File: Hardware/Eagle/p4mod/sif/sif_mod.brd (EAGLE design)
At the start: 19.1 x 11.6 mm, 37 parts, among them Q1 IRLML0030, Q2 IRLML0030, Q3 IRLML0030, Q4 IRLML0030

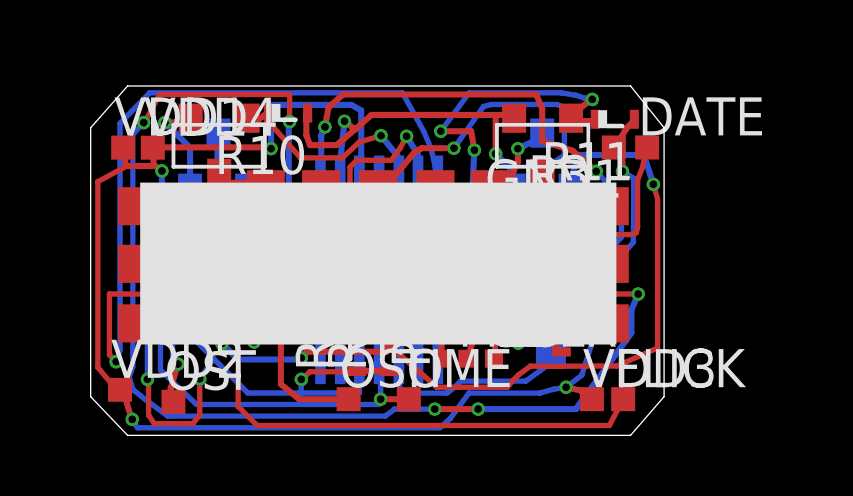
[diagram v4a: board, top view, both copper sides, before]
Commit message: Improved segment resistor values.
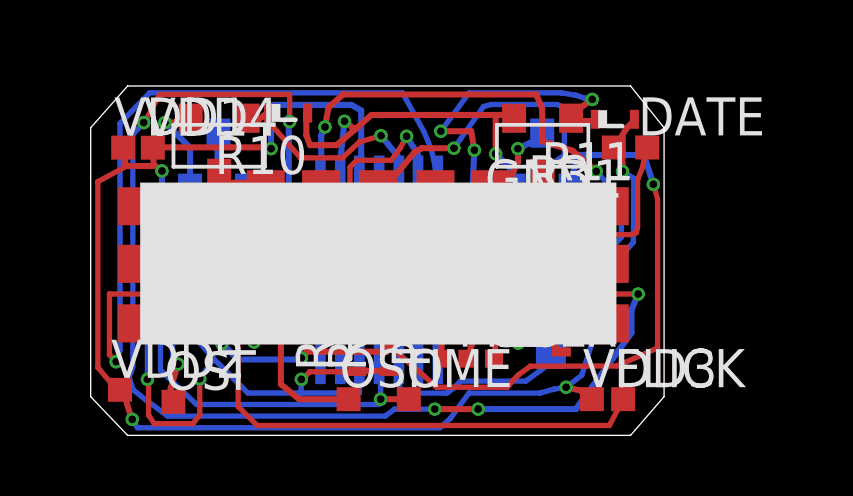
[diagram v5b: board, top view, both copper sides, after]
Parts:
- R2, R3, R4, R5, R6, R7, R8: value 82 -> 75
- moved C1 0.20 mm to (5.05, 4.16)
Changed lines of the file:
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@@
 </element>
 <element name="R1" library="resistor_mod" package="R0402" value="10K" x="18.35831875" y="4.3688" rot="MR90"/>
-<element name="C2" library="resistor_mod" package="C0402K" value="0.1 uF" x="4.553640625" y="7.308175" rot="MR180"/>
+<element name="C2" library="resistor_mod" package="C0402K" value="0.1 uF" x="4.553640625" y="7.3348625" rot="MR180"/>
 <element name="CEFC" library="rcl" package="C0603" value="10 uF" x="16.90450625" y="3.814696875" rot="MR90"/>
-<element name="R2" library="resistor_mod" package="R0402" value="82" x="13.008109375" y="6.29623125"/>
-<element name="R3" library="resistor_mod" package="R0402" value="82" x="16.778290625" y="7.4951875"/>
-<element name="R4" library="resistor_mod" package="R0402" value="82" x="5.038421875" y="4.174128125" rot="R270"/>
-<element name="R5" library="resistor_mod" package="R0402" value="82" x="17.252953125" y="5.629190625" rot="R90"/>
-<element name="R6" library="resistor_mod" package="R0402" value="82" x="17.252953125" y="3.62104375" rot="R90"/>
-<element name="R7" library="resistor_mod" package="R0402" value="82" x="4.9276" y="6.174871875" rot="R270"/>
-<element name="R8" library="resistor_mod" package="R0402" value="82" x="9.549" y="6.708275" rot="R180"/>
+<element name="R2" library="resistor_mod" package="R0402" value="75" x="13.008109375" y="6.29623125"/>
+<element name="R3" library="resistor_mod" package="R0402" value="75" x="16.778290625" y="7.4951875"/>
+<element name="R4" library="resistor_mod" package="R0402" value="75" x="5.038421875" y="4.174128125" rot="R270"/>
+<element name="R5" library="resistor_mod" package="R0402" value="75" x="17.252953125" y="5.629190625" rot="R90"/>
+<element name="R6" library="resistor_mod" package="R0402" value="75" x="17.252953125" y="3.62104375" rot="R90"/>
+<element name="R7" library="resistor_mod" package="R0402" value="75" x="4.9276" y="6.174871875" rot="R270"/>
+<element name="R8" library="resistor_mod" package="R0402" value="75" x="9.549" y="6.708275" rot="R180"/>
 <element name="C4" library="resistor_mod" package="C0402K" value="12 pF" x="4.85618125" y="6.03475" rot="MR90"/>
 <element name="R16" library="resistor_mod" package="R0402" value="4.7k" x="18.35831875" y="6.402271875" rot="MR270"/>
@@
 <attribute name="TP_SIGNAL_NAME" value="" x="18.9992" y="9.787525" size="1.778" layer="27" rot="R180" display="off"/>
 </element>
-<element name="C1" library="resistor_mod" package="C0402K" value="12 pF" x="4.84966875" y="4.17638125" rot="MR270"/>
+<element name="C1" library="resistor_mod" package="C0402K" value="12 pF" x="5.049746875" y="4.1630375" rot="MR270"/>
 <element name="U$2" library="pulsar_p4_display" package="PULSAR_P3_LED_DISPLAY" value="PULSAR_P4_DISPLAYPULSAR_P4_LED_DISPLAY" x="3.21241875" y="3.21965625"/>
 <element name="VDD2" library="testpad" package="TP08SQ" value="TPTP08SQ" x="2.5390625" y="1.708484375">
@@
 <wire x1="5.1308" y1="7.2898" x2="5.1308" y2="6.9088" width="0.2032" layer="16"/>
 <wire x1="4.8768" y1="6.6548" x2="4.85618125" y2="6.63475" width="0.1524" layer="16"/>
-<wire x1="5.1308" y1="7.2898" x2="5.153640625" y2="7.308175" width="0.1524" layer="16"/>
+<wire x1="5.1308" y1="7.2898" x2="5.153640625" y2="7.3348625" width="0.1524" layer="16"/>
 <wire x1="4.8006" y1="6.6548" x2="4.0894" y2="6.6548" width="0.2032" layer="16"/>
 <wire x1="4.0894" y1="6.6548" x2="4.07449375" y2="6.649225" width="0.1524" layer="16"/>
@@
 <wire x1="5.1054" y1="7.366" x2="5.1054" y2="8.4074" width="0.2032" layer="16"/>
 <wire x1="4.9022" y1="8.6106" x2="4.875296875" y2="8.429753125" width="0.1524" layer="16"/>
-<wire x1="5.1054" y1="7.366" x2="5.153640625" y2="7.308175" width="0.2032" layer="16"/>
+<wire x1="5.1054" y1="7.366" x2="5.153640625" y2="7.3348625" width="0.2032" layer="16"/>
 <wire x1="4.4040625" y1="10.62851875" x2="4.8768" y2="10.4648" width="0.2032" layer="1"/>
 <wire x1="4.0386" y1="10.6172" x2="4.4040625" y2="10.62851875" width="0.2032" layer="1"/>
@@
 <wire x1="11.4808" y1="2.3368" x2="11.504365625" y2="2.32038125" width="0.1524" layer="1"/>
 <wire x1="6.80068125" y1="1.604009375" x2="5.6642" y2="2.7432" width="0.1778" layer="16"/>
-<wire x1="5.6642" y1="2.7432" x2="4.8514" y2="3.556" width="0.1778" layer="16"/>
+<wire x1="5.6642" y1="2.7432" x2="4.998121875" y2="3.49595" width="0.1778" layer="16"/>
 <wire x1="10.52211875" y1="1.604009375" x2="8.57868125" y2="1.604009375" width="0.1778" layer="16"/>
 <wire x1="8.57868125" y1="1.604009375" x2="6.80068125" y2="1.604009375" width="0.1778" layer="16"/>
 <wire x1="10.5156" y1="2.6416" x2="10.52211875" y2="1.604009375" width="0.1778" layer="16"/>
-<wire x1="4.8514" y1="3.556" x2="4.84966875" y2="3.57638125" width="0.1524" layer="16"/>
+<wire x1="4.998121875" y1="3.49595" x2="5.049746875" y2="3.5630375" width="0.2032" layer="16"/>
 <wire x1="10.5156" y1="2.6416" x2="10.51689375" y2="2.6595375" width="0.1524" layer="16"/>
 <wire x1="8.8646" y1="2.3114" x2="10.3632" y2="2.3114" width="0.1778" layer="1"/>
@@
 <wire x1="3.6576" y1="9.2202" x2="3.937" y2="9.0056125" width="0.2032" layer="1"/>
 <wire x1="3.6576" y1="9.779" x2="3.6576" y2="9.2202" width="0.2032" layer="1"/>
-<wire x1="3.937" y1="7.3152" x2="3.953640625" y2="7.308175" width="0.1524" layer="16"/>
+<wire x1="3.937" y1="7.3152" x2="3.953640625" y2="7.3348625" width="0.1524" layer="16"/>
 <wire x1="3.6576" y1="9.779" x2="3.633571875" y2="9.779" width="0.1778" layer="1"/>
 <wire x1="1.801746875" y1="2.453284375" x2="2.6924" y2="1.397" width="0.1778" layer="1"/>
@@
 <contactref element="OSI" pad="TP"/>
 <contactref element="C1" pad="1"/>
-<wire x1="5.569715625" y1="4.151021875" x2="5.0038" y2="4.6228" width="0.1778" layer="16"/>
-<wire x1="5.0038" y1="4.6228" x2="4.8514" y2="4.7752" width="0.1778" layer="16"/>
+<wire x1="5.569715625" y1="4.151021875" x2="5.043815625" y2="4.689521875" width="0.1778" layer="16"/>
+<wire x1="5.043815625" y1="4.689521875" x2="5.03146875" y2="4.695134375" width="0.1778" layer="16"/>
 <wire x1="6.009815625" y1="3.8597625" x2="5.569715625" y2="4.151021875" width="0.1778" layer="16"/>
 <wire x1="6.301965625" y1="3.7084" x2="6.009815625" y2="3.8597625" width="0.1778" layer="16"/>
@@
 <wire x1="7.366" y1="4.353446875" x2="6.6802" y2="3.7084" width="0.1778" layer="16"/>
 <wire x1="8.128" y1="4.3942" x2="7.366" y2="4.353446875" width="0.1778" layer="16"/>
-<wire x1="4.8514" y1="4.7752" x2="4.84966875" y2="4.77638125" width="0.1524" layer="16"/>
+<wire x1="5.03146875" y1="4.695134375" x2="5.049746875" y2="4.7630375" width="0.1524" layer="16"/>
 <wire x1="8.128" y1="4.3942" x2="8.12929375" y2="4.4121375" width="0.1524" layer="16"/>
 <wire x1="4.228509375" y1="1.753315625" x2="4.2418" y2="1.397" width="0.2032" layer="1"/>
@@
 <wire x1="4.2926" y1="2.7686" x2="4.4704" y2="2.56823125" width="0.1778" layer="16"/>
 <wire x1="4.2926" y1="4.490115625" x2="4.2926" y2="2.7686" width="0.1778" layer="16"/>
-<wire x1="5.0038" y1="4.6228" x2="4.2926" y2="4.490115625" width="0.1778" layer="16"/>
+<wire x1="5.043815625" y1="4.689521875" x2="4.2926" y2="4.490115625" width="0.1778" layer="16"/>
 <wire x1="4.2418" y1="1.397" x2="4.321521875" y2="1.310065625" width="0.2032" layer="1"/>
 <via x="4.4704" y="2.56823125" extent="1-16" drill="0.254"/>
